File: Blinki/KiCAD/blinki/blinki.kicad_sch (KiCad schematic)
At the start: 10 parts, among them Q1 Q_NPN_CBE, Q2 Q_NPN_CBE

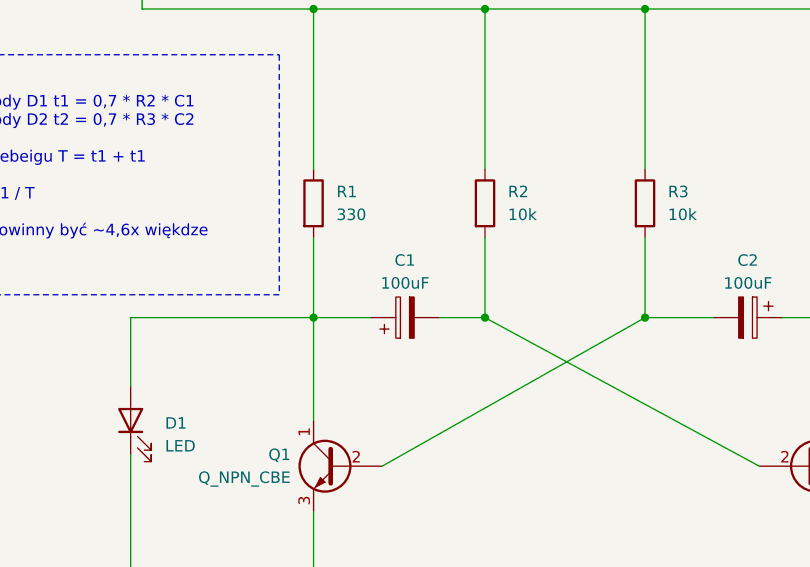
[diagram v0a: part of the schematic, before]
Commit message: Adds info for simulation.
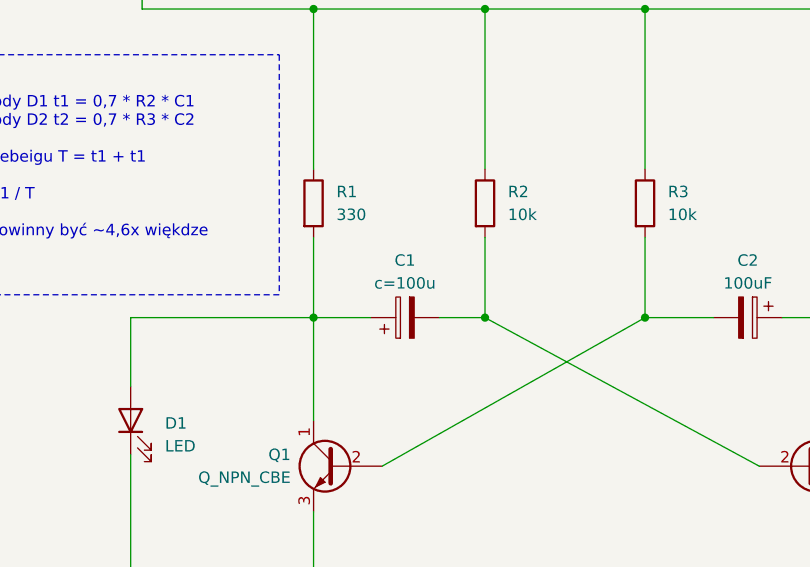
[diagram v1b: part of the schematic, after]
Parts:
- C1: value 100uF -> ${SIM.PARAMS}
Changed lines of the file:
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@@
+      (effects (font (size 1.27 1.27)) hide)
+    )
+    (property "Sim.Device" "NPN" (at 119.38 104.14 0)
+      (effects (font (size 1.27 1.27)) hide)
+    )
+    (property "Sim.Type" "VBIC" (at 119.38 104.14 0)
+      (effects (font (size 1.27 1.27)) hide)
+    )
+    (property "Sim.Pins" "1=C 2=B 3=E" (at 119.38 104.14 0)
       (effects (font (size 1.27 1.27)) hide)
     )
@@
       (effects (font (size 1.27 1.27)) hide)
     )
+    (property "Sim.Device" "V" (at 97.79 50.8 0)
+      (effects (font (size 1.27 1.27)) hide)
+    )
+    (property "Sim.Type" "DC" (at 97.79 50.8 0)
+      (effects (font (size 1.27 1.27)) hide)
+    )
+    (property "Sim.Pins" "1=+" (at 97.79 50.8 0)
+      (effects (font (size 1.27 1.27)) hide)
+    )
+    (property "Sim.Params" "dc=5" (at 97.79 50.8 0)
+      (effects (font (size 1.27 1.27)) hide)
+    )
     (pin "1")
     (instances
@@
     )
     (property "Datasheet" "~" (at 96.52 99.06 0)
+      (effects (font (size 1.27 1.27)) hide)
+    )
+    (property "Sim.Device" "D" (at 96.52 99.06 0)
+      (effects (font (size 1.27 1.27)) hide)
+    )
+    (property "Sim.Pins" "1=A 2=K" (at 96.52 99.06 0)
       (effects (font (size 1.27 1.27)) hide)
     )
@@
       (effects (font (size 1.27 1.27)) hide)
     )
+    (property "Sim.Device" "NPN" (at 171.45 104.14 0)
+      (effects (font (size 1.27 1.27)) hide)
+    )
+    (property "Sim.Type" "VBIC" (at 171.45 104.14 0)
+      (effects (font (size 1.27 1.27)) hide)
+    )
+    (property "Sim.Pins" "1=C 2=B 3=E" (at 171.45 104.14 0)
+      (effects (font (size 1.27 1.27)) hide)
+    )
     (pin "1")
     (pin "2")
@@
     )
     (property "Datasheet" "~" (at 194.31 99.06 0)
+      (effects (font (size 1.27 1.27)) hide)
+    )
+    (property "Sim.Device" "D" (at 194.31 99.06 0)
+      (effects (font (size 1.27 1.27)) hide)
+    )
+    (property "Sim.Pins" "1=A 2=K" (at 194.31 99.06 0)
       (effects (font (size 1.27 1.27)) hide)
     )
@@
       (effects (font (size 1.27 1.27)))
     )
-    (property "Value" "100uF" (at 127 83.82 90)
+    (property "Value" "${SIM.PARAMS}" (at 127 83.82 90)
       (effects (font (size 1.27 1.27)))
     )
@@
       (effects (font (size 1.27 1.27)) hide)
     )
+    (property "Sim.Device" "C" (at 127 87.63 0)
+      (effects (font (size 1.27 1.27)) hide)
+    )
+    (property "Sim.Params" "c=100u" (at 127 87.63 0)
+      (effects (font (size 1.27 1.27)) hide)
+    )
+    (property "Sim.Pins" "1=+ 2=-" (at 127 87.63 0)
+      (effects (font (size 1.27 1.27)) hide)
+    )

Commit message: Adds layout.
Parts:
- C1, C2: footprint (none) -> Capacitor_THT:CP_Radial_D8.0mm_P5.00mm
- D1, D2: footprint (none) -> LED_THT:LED_D5.0mm
- Q1, Q2: footprint (none) -> Package_TO_SOT_THT:TO-92_Inline_Wide
- R1, R2, R3, R4: footprint (none) -> Resistor_THT:R_Axial_DIN0204_L3.6mm_D1.6mm_P1.90mm_Vertical
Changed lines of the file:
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@@
       (effects (font (size 1.27 1.27)) (justify left))
     )
-    (property "Footprint" "" (at 151.892 74.93 90)
+    (property "Footprint" "Resistor_THT:R_Axial_DIN0204_L3.6mm_D1.6mm_P1.90mm_Vertical" (at 151.892 74.93 90)
       (effects (font (size 1.27 1.27)) hide)
     )
@@
       (effects (font (size 1.27 1.27)) (justify left))
     )
-    (property "Footprint" "" (at 115.062 74.93 90)
+    (property "Footprint" "Resistor_THT:R_Axial_DIN0204_L3.6mm_D1.6mm_P1.90mm_Vertical" (at 115.062 74.93 90)
       (effects (font (size 1.27 1.27)) hide)
     )
@@
       (effects (font (size 1.27 1.27)) (justify left))
     )
-    (property "Footprint" "" (at 172.212 74.93 90)
+    (property "Footprint" "Resistor_THT:R_Axial_DIN0204_L3.6mm_D1.6mm_P1.90mm_Vertical" (at 172.212 74.93 90)
       (effects (font (size 1.27 1.27)) hide)
     )
@@
       (effects (font (size 1.27 1.27)) (justify left))
     )
-    (property "Footprint" "" (at 114.3 101.6 0)
+    (property "Footprint" "Package_TO_SOT_THT:TO-92_Inline_Wide" (at 114.3 101.6 0)
       (effects (font (size 1.27 1.27)) hide)
     )
@@
       (effects (font (size 1.27 1.27)))
     )
-    (property "Footprint" "" (at 161.29 88.5952 0)
+    (property "Footprint" "Capacitor_THT:CP_Radial_D8.0mm_P5.00mm" (at 161.29 88.5952 0)
       (effects (font (size 1.27 1.27)) hide)
     )
@@
       (effects (font (size 1.27 1.27)) (justify right))
     )
-    (property "Footprint" "" (at 96.52 99.06 0)
+    (property "Footprint" "LED_THT:LED_D5.0mm" (at 96.52 99.06 0)
       (effects (font (size 1.27 1.27)) hide)
     )
@@
       (effects (font (size 1.27 1.27)) (justify left))
     )
-    (property "Footprint" "" (at 176.53 101.6 0)
+    (property "Footprint" "Package_TO_SOT_THT:TO-92_Inline_Wide" (at 176.53 101.6 0)
       (effects (font (size 1.27 1.27)) hide)
     )
@@
       (effects (font (size 1.27 1.27)) (justify right))
     )
-    (property "Footprint" "" (at 194.31 99.06 0)
+    (property "Footprint" "LED_THT:LED_D5.0mm" (at 194.31 99.06 0)
       (effects (font (size 1.27 1.27)) hide)
     )
@@
       (effects (font (size 1.27 1.27)))
     )
-    (property "Footprint" "" (at 130.81 86.6648 0)
+    (property "Footprint" "Capacitor_THT:CP_Radial_D8.0mm_P5.00mm" (at 130.81 86.6648 0)
       (effects (font (size 1.27 1.27)) hide)
     )
@@
       (effects (font (size 1.27 1.27)) (justify left))
     )
-    (property "Footprint" "" (at 134.112 74.93 90)
-      (effects (font (size 1.27 1.27)) hide)
-    )
+    (property "Footprint" "Resistor_THT:R_Axial_DIN0204_L3.6mm_D1.6mm_P1.90mm_Vertical" (at 134.112 74.93 90)
+      (effects (font (size 1.27 1.27)) hide)
+    )
